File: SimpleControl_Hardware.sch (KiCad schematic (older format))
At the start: 34 parts, among them J1 Jack-DC, J2 AudioJack3, SW1 SW_SPDT, U1 MCP3208, U2 ProMicro, U3 CD74HC154M96, U4 MCP23017_SO, U5 CD74HC154M96, U6 CD74HC154M96

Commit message: correct symbols/footprints
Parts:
- added TP1, TP10, TP11, TP12, TP13, TP14, TP2, TP3, TP4, TP5, TP6, TP7, TP8, TP9: TestPoint, SimpleControl_Hardware:TP_1PAD, symbol Connector:TestPoint
- J2: footprint SimpleControl_Hardware:CUI_SJ-3523-SMT-TR -> SimpleControl_Hardware:CUI_SJ-3523-SMT-TR_TRS
- S1: footprint digikey-footprints:Switch_Tactile_SMD_B3U-1000P -> SimpleControl_Hardware:SW_Tactile_Akizuki
- U1: footprint Housings_SOIC:SOIC-14_3.9x8.7mm_Pitch1.27mm -> Housings_SOIC:SOIC-16_3.9x9.9mm_Pitch1.27mm
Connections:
- net CS_0: now also TP10.1
- net DECODER_A0: now also TP5.1, TP7.1
- net DECODER_A1: now also TP9.1
- net DECODER_A2: now also TP11.1
- net DECODER_A3: now also TP12.1
- net DECODER_EN0: now also TP13.1
- net DECODER_EN1: now also TP14.1
- net GND: now also TP1.1
- net MISO: now also TP6.1
- net MOSI: now also TP8.1
- net SCK: now also TP4.1
- net SCL: now also TP3.1
- net SDA: now also TP2.1
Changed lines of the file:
@@
 F 0 "U1" H 11200 5600 50  0000 C CNN
 F 1 "MCP3208" H 11200 5500 50  0000 C CNN
-F 2 "Housings_SOIC:SOIC-14_3.9x8.7mm_Pitch1.27mm" H 11300 4750 50  0001 C CNN
+F 2 "Housings_SOIC:SOIC-16_3.9x9.9mm_Pitch1.27mm" H 11300 4750 50  0001 C CNN
 F 3 "http://ww1.microchip.com/downloads/en/DeviceDoc/21298c.pdf" H 11300 4750 50  0001 C CNN
 	1    11200 4650
@@
 	1750 3100 1750 2950
 Wire Wire Line
-	1750 3100 2650 3100
-Wire Wire Line
-	2650 3200 1500 3200
+	1750 3100 1950 3100
+Wire Wire Line
+	2650 3200 1950 3200
 Wire Wire Line
 	1500 3200 1500 2950
@@
 F 0 "J2" H 13670 1233 50  0000 R CNN
 F 1 "AudioJack3" H 13670 1324 50  0000 R CNN
-F 2 "SimpleControl_Hardware:CUI_SJ-3523-SMT-TR" H 13950 1300 50  0001 C CNN
+F 2 "SimpleControl_Hardware:CUI_SJ-3523-SMT-TR_TRS" H 13950 1300 50  0001 C CNN
 F 3 "~" H 13950 1300 50  0001 C CNN
 	1    13950 1300
@@
 Wire Wire Line
 	14400 6750 14350 6750
-Text GLabel 4050 3600 2    50   Input ~ 0
-MISO
-Text GLabel 4050 3700 2    50   Output ~ 0
-MOSI
-Text GLabel 4050 3500 2    50   Output ~ 0
-SCK
 $Comp
 L Device:C C2
@@
 F 0 "S1" V 5247 3538 60  0000 L CNN
 F 1 "B3U-1000P" V 5353 3538 60  0000 L CNN
-F 2 "digikey-footprints:Switch_Tactile_SMD_B3U-1000P" H 5500 3600 60  0001 L CNN
+F 2 "SimpleControl_Hardware:SW_Tactile_Akizuki" H 5500 3600 60  0001 L CNN
 F 3 "https://omronfs.omron.com/en_US/ecb/products/pdf/en-b3u.pdf" H 5500 3700 60  0001 L CNN
 F 4 "SW1020CT-ND" H 5500 3800 60  0001 L CNN "Digi-Key_PN"
@@
 $EndComp
 Wire Wire Line
-	1750 1500 1450 1500
+	1750 1500 1650 1500
 Connection ~ 1450 1500
+$Comp
+L Connector:TestPoint TP2
+U 1 1 5DEB79E6
+P 1950 3100
+F 0 "TP2" H 1950 3450 50  0000 L CNN
+F 1 "TestPoint" H 1950 3350 50  0000 L CNN
+F 2 "SimpleControl_Hardware:TP_1PAD" H 2150 3100 50  0001 C CNN
+F 3 "~" H 2150 3100 50  0001 C CNN
+	1    1950 3100
+	1    0    0    -1
+$EndComp
+Connection ~ 1950 3100
+Wire Wire Line
+	1950 3100 2650 3100
+$Comp
+L Connector:TestPoint TP3
+U 1 1 5DEB8D26
+P 1950 3200
+F 0 "TP3" H 2150 3350 50  0000 R CNN
+F 1 "TestPoint" H 2200 3450 50  0000 R CNN
+F 2 "SimpleControl_Hardware:TP_1PAD" H 2150 3200 50  0001 C CNN
+F 3 "~" H 2150 3200 50  0001 C CNN
+	1    1950 3200
+	-1   0    0    1
+$EndComp
+Connection ~ 1950 3200
+Wire Wire Line
+	1950 3200 1500 3200
+$Comp
+L Connector:TestPoint TP1
+U 1 1 5DEBA08B
+P 1650 1500
+F 0 "TP1" H 1600 1700 50  0000 R CNN
+F 1 "TestPoint" H 1600 1750 50  0000 R CNN
+F 2 "SimpleControl_Hardware:TP_1PAD" H 1850 1500 50  0001 C CNN
+F 3 "~" H 1850 1500 50  0001 C CNN
+	1    1650 1500
+	-1   0    0    1
+$EndComp
+Connection ~ 1650 1500
+Wire Wire Line
+	1650 1500 1450 1500
+Text GLabel 4050 3500 2    50   Output ~ 0
+SCK
+Text GLabel 4050 3700 2    50   Output ~ 0
+MOSI
+Text GLabel 4050 3600 2    50   Input ~ 0
+MISO
+Text GLabel 9250 4350 0    50   Input ~ 0
+SCK
+Text GLabel 9250 4600 0    50   Input ~ 0
+MISO
+Text GLabel 9250 4850 0    50   Input ~ 0
+MOSI
+Text GLabel 9250 5100 0    50   Input ~ 0
+CS_0
+$Comp
+L Connector:TestPoint TP4
+U 1 1 5DEC29B7
+P 9250 4350
+F 0 "TP4" V 9204 4538 50  0000 L CNN
+F 1 "TestPoint" V 9295 4538 50  0000 L CNN
+F 2 "SimpleControl_Hardware:TP_1PAD" H 9450 4350 50  0001 C CNN
+F 3 "~" H 9450 4350 50  0001 C CNN
+	1    9250 4350
+	0    1    1    0
+$EndComp
+$Comp
+L Connector:TestPoint TP6
+U 1 1 5DEC4003
+P 9250 4600
+F 0 "TP6" V 9204 4788 50  0000 L CNN
+F 1 "TestPoint" V 9295 4788 50  0000 L CNN
+F 2 "SimpleControl_Hardware:TP_1PAD" H 9450 4600 50  0001 C CNN
+F 3 "~" H 9450 4600 50  0001 C CNN
+	1    9250 4600
+	0    1    1    0
+$EndComp
+$Comp
+L Connector:TestPoint TP8
+U 1 1 5DEC43C9
+P 9250 4850
+F 0 "TP8" V 9204 5038 50  0000 L CNN
+F 1 "TestPoint" V 9295 5038 50  0000 L CNN
+F 2 "SimpleControl_Hardware:TP_1PAD" H 9450 4850 50  0001 C CNN
+F 3 "~" H 9450 4850 50  0001 C CNN
+	1    9250 4850
+	0    1    1    0
+$EndComp
+$Comp
+L Connector:TestPoint TP10
+U 1 1 5DEC477B
+P 9250 5100
+F 0 "TP10" V 9204 5288 50  0000 L CNN
+F 1 "TestPoint" V 9295 5288 50  0000 L CNN
+F 2 "SimpleControl_Hardware:TP_1PAD" H 9450 5100 50  0001 C CNN
+F 3 "~" H 9450 5100 50  0001 C CNN
+	1    9250 5100
+	0    1    1    0
+$EndComp
+Text GLabel 2100 4750 0    50   Input ~ 0
+DECODER_A0
+Text GLabel 2100 5050 0    50   Input ~ 0
+DECODER_A1
+Text GLabel 2100 5350 0    50   Input ~ 0
+DECODER_A2
+Text GLabel 2100 5650 0    50   Input ~ 0
+DECODER_A3
+Text GLabel 2100 5950 0    50   Input ~ 0
+DECODER_EN0
+Text GLabel 2100 6200 0    50   Input ~ 0
+DECODER_EN1
+Text GLabel 2100 4500 0    50   Input ~ 0
+DECODER_A0
+$Comp
+L Connector:TestPoint TP5
+U 1 1 5DEDEFC3
+P 2100 4500
+F 0 "TP5" V 2054 4688 50  0000 L CNN
+F 1 "TestPoint" V 2145 4688 50  0000 L CNN
+F 2 "SimpleControl_Hardware:TP_1PAD" H 2300 4500 50  0001 C CNN
+F 3 "~" H 2300 4500 50  0001 C CNN
+	1    2100 4500
+	0    1    1    0
+$EndComp
+$Comp
+L Connector:TestPoint TP7
+U 1 1 5DEDFBBC
+P 2100 4750
+F 0 "TP7" V 2054 4938 50  0000 L CNN
+F 1 "TestPoint" V 2145 4938 50  0000 L CNN
+F 2 "SimpleControl_Hardware:TP_1PAD" H 2300 4750 50  0001 C CNN
+F 3 "~" H 2300 4750 50  0001 C CNN
+	1    2100 4750
+	0    1    1    0
+$EndComp
+$Comp
+L Connector:TestPoint TP9
+U 1 1 5DEDFE2A
+P 2100 5050
+F 0 "TP9" V 2054 5238 50  0000 L CNN
+F 1 "TestPoint" V 2145 5238 50  0000 L CNN
+F 2 "SimpleControl_Hardware:TP_1PAD" H 2300 5050 50  0001 C CNN
+F 3 "~" H 2300 5050 50  0001 C CNN
+	1    2100 5050
+	0    1    1    0
+$EndComp
+$Comp
+L Connector:TestPoint TP11
+U 1 1 5DEE032B
+P 2100 5350
+F 0 "TP11" V 2054 5538 50  0000 L CNN
+F 1 "TestPoint" V 2145 5538 50  0000 L CNN
+F 2 "SimpleControl_Hardware:TP_1PAD" H 2300 5350 50  0001 C CNN
+F 3 "~" H 2300 5350 50  0001 C CNN
+	1    2100 5350
+	0    1    1    0
+$EndComp
+$Comp
+L Connector:TestPoint TP12
+U 1 1 5DEE077B
+P 2100 5650
+F 0 "TP12" V 2054 5838 50  0000 L CNN
+F 1 "TestPoint" V 2145 5838 50  0000 L CNN
+F 2 "SimpleControl_Hardware:TP_1PAD" H 2300 5650 50  0001 C CNN
+F 3 "~" H 2300 5650 50  0001 C CNN
+	1    2100 5650
+	0    1    1    0
+$EndComp
+$Comp
+L Connector:TestPoint TP13
+U 1 1 5DEE0C4A
+P 2100 5950
+F 0 "TP13" V 2054 6138 50  0000 L CNN
+F 1 "TestPoint" V 2145 6138 50  0000 L CNN
+F 2 "SimpleControl_Hardware:TP_1PAD" H 2300 5950 50  0001 C CNN
+F 3 "~" H 2300 5950 50  0001 C CNN
+	1    2100 5950
+	0    1    1    0
+$EndComp
+$Comp
+L Connector:TestPoint TP14
+U 1 1 5DEE0F8D
+P 2100 6200
+F 0 "TP14" V 2054 6388 50  0000 L CNN
+F 1 "TestPoint" V 2145 6388 50  0000 L CNN
+F 2 "SimpleControl_Hardware:TP_1PAD" H 2300 6200 50  0001 C CNN
+F 3 "~" H 2300 6200 50  0001 C CNN
+	1    2100 6200
+	0    1    1    0
+$EndComp
 $EndSCHEMATC

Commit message: layouting pcb, add initial prototype for reference
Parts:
- removed R4: 10k, Resistors_SMD:R_0603_HandSoldering, symbol Device:R
- removed TP5: TestPoint, SimpleControl_Hardware:TP_1PAD, symbol Connector:TestPoint
- added H1, H2, H3, H4: MountingHole, Mounting_Holes:MountingHole_3.2mm_M3_DIN965_Pad, symbol Mechanical:MountingHole
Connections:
- net at U2.22 (RST): now also S1.1
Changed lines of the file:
@@
-	1    0    0    -1
-$EndComp
-$Comp
-L Device:R R4
-U 1 1 5DEDC536
-P 5300 3050
-F 0 "R4" H 5370 3096 50  0000 L CNN
-F 1 "10k" H 5370 3005 50  0000 L CNN
-F 2 "Resistors_SMD:R_0603_HandSoldering" V 5230 3050 50  0001 C CNN
-F 3 "~" H 5300 3050 50  0001 C CNN
-	1    5300 3050
 	1    0    0    -1
 $EndComp
@@
 Text GLabel 2100 6200 0    50   Input ~ 0
 DECODER_EN1
-Text GLabel 2100 4500 0    50   Input ~ 0
-DECODER_A0
-$Comp
-L Connector:TestPoint TP5
-U 1 1 5DEDEFC3
-P 2100 4500
-F 0 "TP5" V 2054 4688 50  0000 L CNN
-F 1 "TestPoint" V 2145 4688 50  0000 L CNN
-F 2 "SimpleControl_Hardware:TP_1PAD" H 2300 4500 50  0001 C CNN
-F 3 "~" H 2300 4500 50  0001 C CNN
-	1    2100 4500
-	0    1    1    0
-$EndComp
 $Comp
 L Connector:TestPoint TP7
@@
 	0    1    1    0
 $EndComp
+Wire Wire Line
+	5300 2900 5300 3200
+$Comp
+L Mechanical:MountingHole H1
+U 1 1 5DF0F4C2
+P 14950 4650
+F 0 "H1" H 15050 4696 50  0000 L CNN
+F 1 "MountingHole" H 15050 4605 50  0000 L CNN
+F 2 "Mounting_Holes:MountingHole_3.2mm_M3_DIN965_Pad" H 14950 4650 50  0001 C CNN
+F 3 "~" H 14950 4650 50  0001 C CNN
+	1    14950 4650
+	1    0    0    -1
+$EndComp
+$Comp
+L Mechanical:MountingHole H2
+U 1 1 5DF0FF46
+P 14950 4900
+F 0 "H2" H 15050 4946 50  0000 L CNN
+F 1 "MountingHole" H 15050 4855 50  0000 L CNN
+F 2 "Mounting_Holes:MountingHole_3.2mm_M3_DIN965_Pad" H 14950 4900 50  0001 C CNN
+F 3 "~" H 14950 4900 50  0001 C CNN
+	1    14950 4900
+	1    0    0    -1
+$EndComp
+$Comp
+L Mechanical:MountingHole H3
+U 1 1 5DF10415
+P 14950 5150
+F 0 "H3" H 15050 5196 50  0000 L CNN
+F 1 "MountingHole" H 15050 5105 50  0000 L CNN
+F 2 "Mounting_Holes:MountingHole_3.2mm_M3_DIN965_Pad" H 14950 5150 50  0001 C CNN
+F 3 "~" H 14950 5150 50  0001 C CNN
+	1    14950 5150
+	1    0    0    -1
+$EndComp
+$Comp
+L Mechanical:MountingHole H4
+U 1 1 5DF10B22
+P 14950 5400
+F 0 "H4" H 15050 5446 50  0000 L CNN
+F 1 "MountingHole" H 15050 5355 50  0000 L CNN
+F 2 "Mounting_Holes:MountingHole_3.2mm_M3_DIN965_Pad" H 14950 5400 50  0001 C CNN
+F 3 "~" H 14950 5400 50  0001 C CNN
+	1    14950 5400
+	1    0    0    -1
+$EndComp
 $EndSCHEMATC

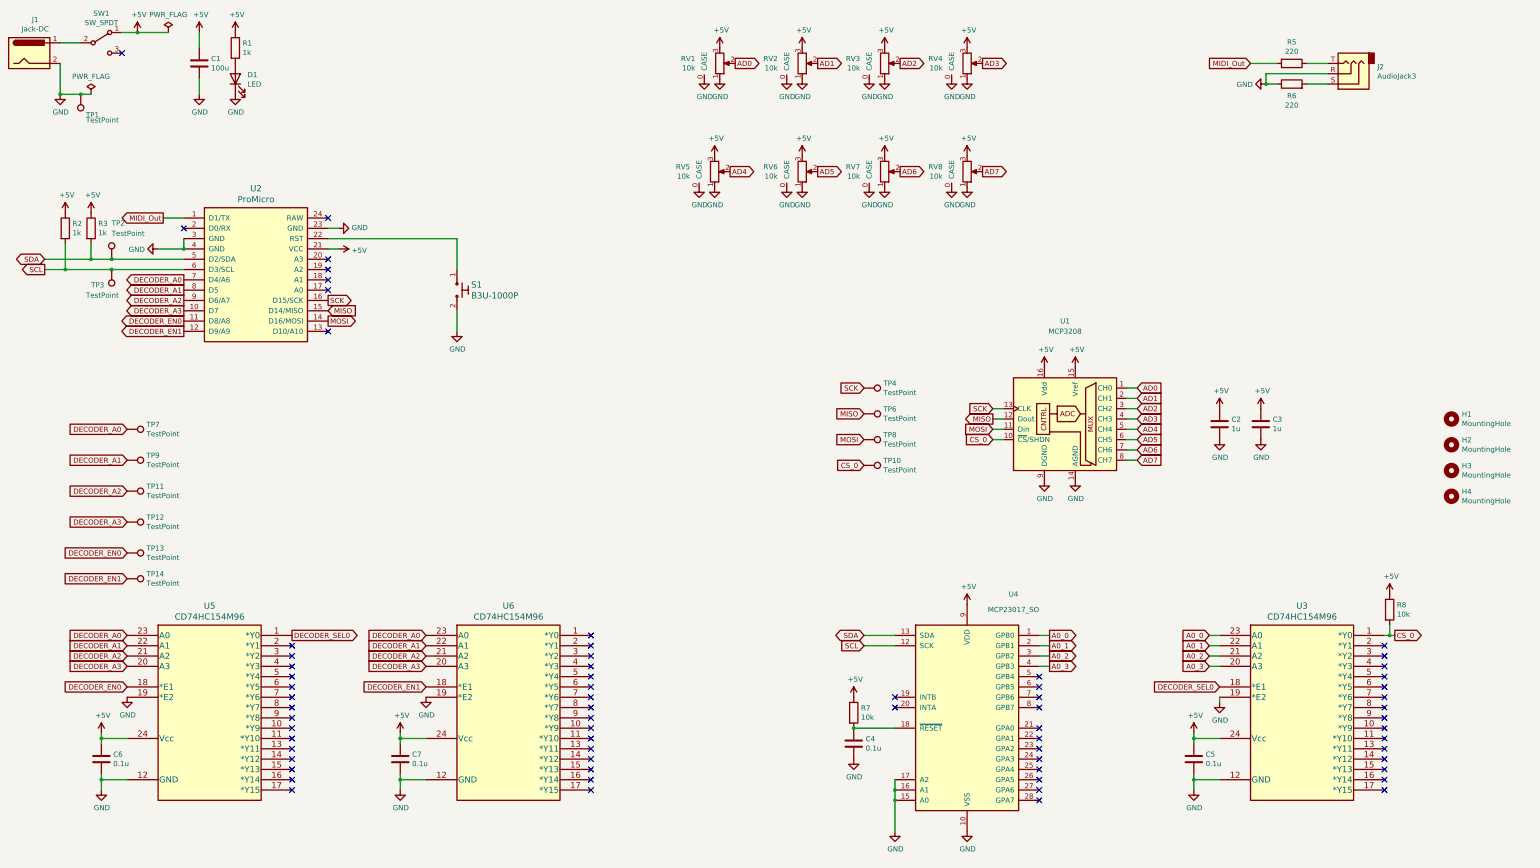
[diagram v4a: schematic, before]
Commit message: add 24 pin connector for extension
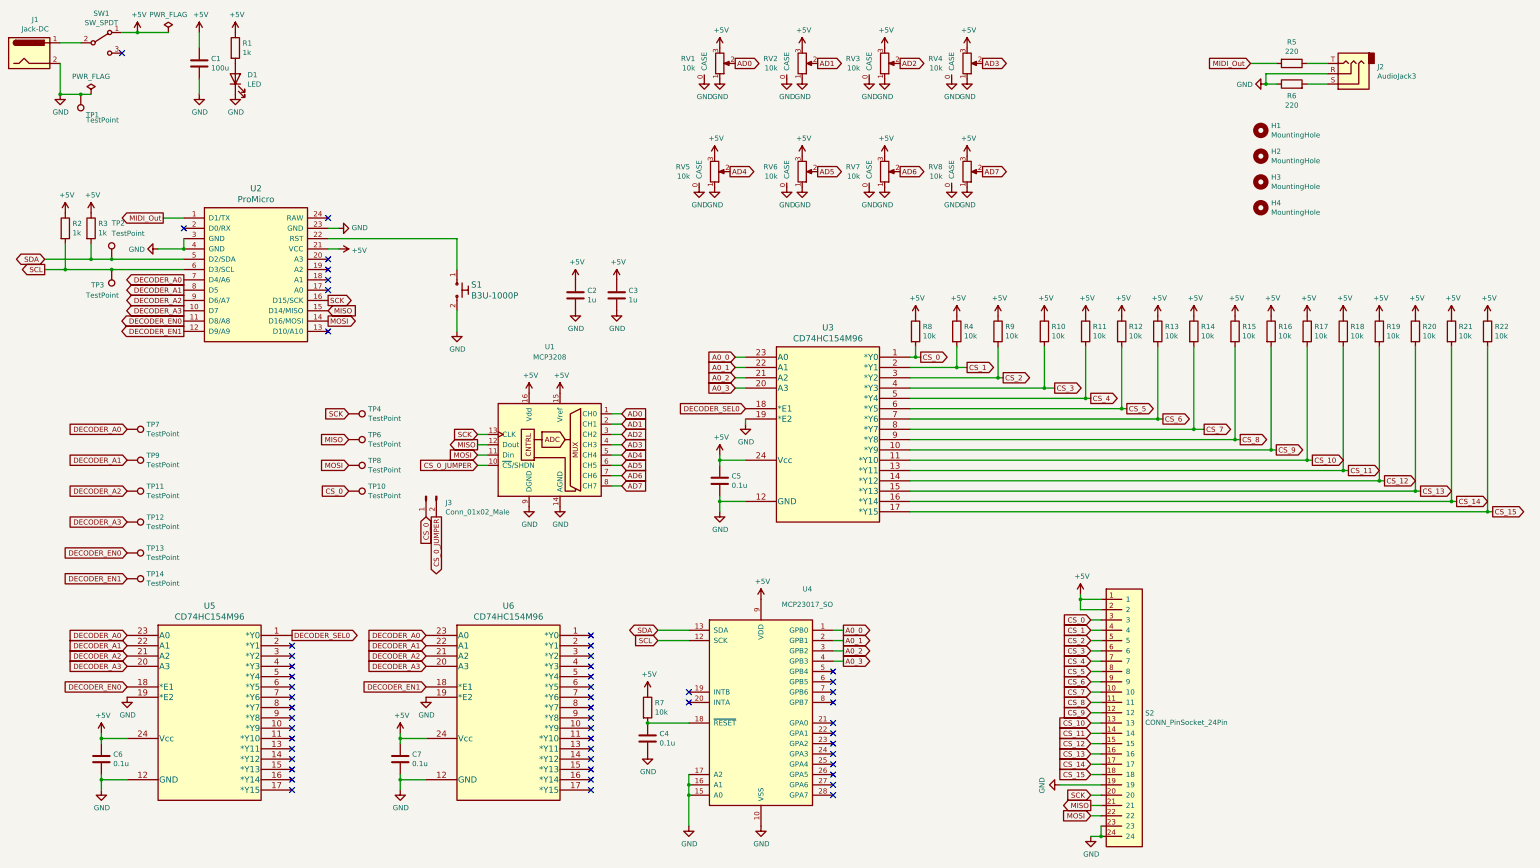
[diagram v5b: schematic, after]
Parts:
- added J3: Conn_01x02_Male, SimpleControl_Hardware:2.54mm_2pin_1pinmark, symbol Connector:Conn_01x02_Male
- added R10, R11, R12, R13, R14, R15, R16, R17, R18, R19, R20, R21, R22, R4, R9: 10k, Resistors_SMD:R_0603_HandSoldering, symbol Device:R
- added S2: CONN_PinSocket_24Pin, SimpleControl_Hardware:CONN_PinSocket_24Pin_2Row, symbol mylib:CONN_PinSocket_24Pin
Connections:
- net +5V: now also R10.1, R11.1, R12.1, R13.1, R14.1, R15.1, R16.1, R17.1, R18.1, R19.1, R20.1, R21.1, R22.1, R4.1, R9.1, S2.1, S2.2
- net CS_0: now also J3.1 (Pin_1), S2.3; no longer U1.10 (~CS~/SHDN)
- net GND: now also S2.19, S2.23, S2.24
- net MISO: now also S2.21
- net MOSI: now also S2.22
- net SCK: now also S2.20
- net CS_9: now reaches U3.10 (*Y9)
- net CS_9: now also R16.2, S2.12
- net CS_10: now reaches U3.11 (*Y10)
- net CS_10: now also R17.2, S2.13
- net CS_11: now reaches U3.13 (*Y11)
- net CS_11: now also R18.2, S2.14
- net CS_12: now reaches U3.14 (*Y12)
- net CS_12: now also R19.2, S2.15
- net CS_13: now reaches U3.15 (*Y13)
- net CS_13: now also R20.2, S2.16
- net CS_14: now reaches U3.16 (*Y14)
- net CS_14: now also R21.2, S2.17
- net CS_15: now reaches U3.17 (*Y15)
- net CS_15: now also R22.2, S2.18
- net CS_1: now reaches U3.2 (*Y1)
- net CS_1: now also R4.2, S2.4
- net CS_2: now reaches U3.3 (*Y2)
- net CS_2: now also R9.2, S2.5
- net CS_3: now reaches U3.4 (*Y3)
- net CS_3: now also R10.2, S2.6
- net CS_4: now reaches U3.5 (*Y4)
- net CS_4: now also R11.2, S2.7
- net CS_5: now reaches U3.6 (*Y5)
- net CS_5: now also R12.2, S2.8
- net CS_6: now reaches U3.7 (*Y6)
- net CS_6: now also R13.2, S2.9
- net CS_7: now reaches U3.8 (*Y7)
- net CS_7: now also R14.2, S2.10
- net CS_8: now reaches U3.9 (*Y8)
- net CS_8: now also R15.2, S2.11
- new net CS_0_JUMPER: J3.2 (Pin_2), U1.10 (~CS~/SHDN)
- no-connect marks 68 -> 53
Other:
- moved on the sheet: C2, C3, C4, C5, H1, H2, H3, H4, R7, R8, TP10, TP4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
